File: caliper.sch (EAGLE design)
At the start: 57 parts, among them IC1 AT90S2313S, IC3 TS5205, IC6 MAX489CSD, Q10 BCX71SMD, Q11 BCX71SMD, Q12 BC817-40SMD, Q13 BC817-40SMD, Q2 BCX71SMD, Q3 BCX71SMD, Q4 BC817-40SMD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

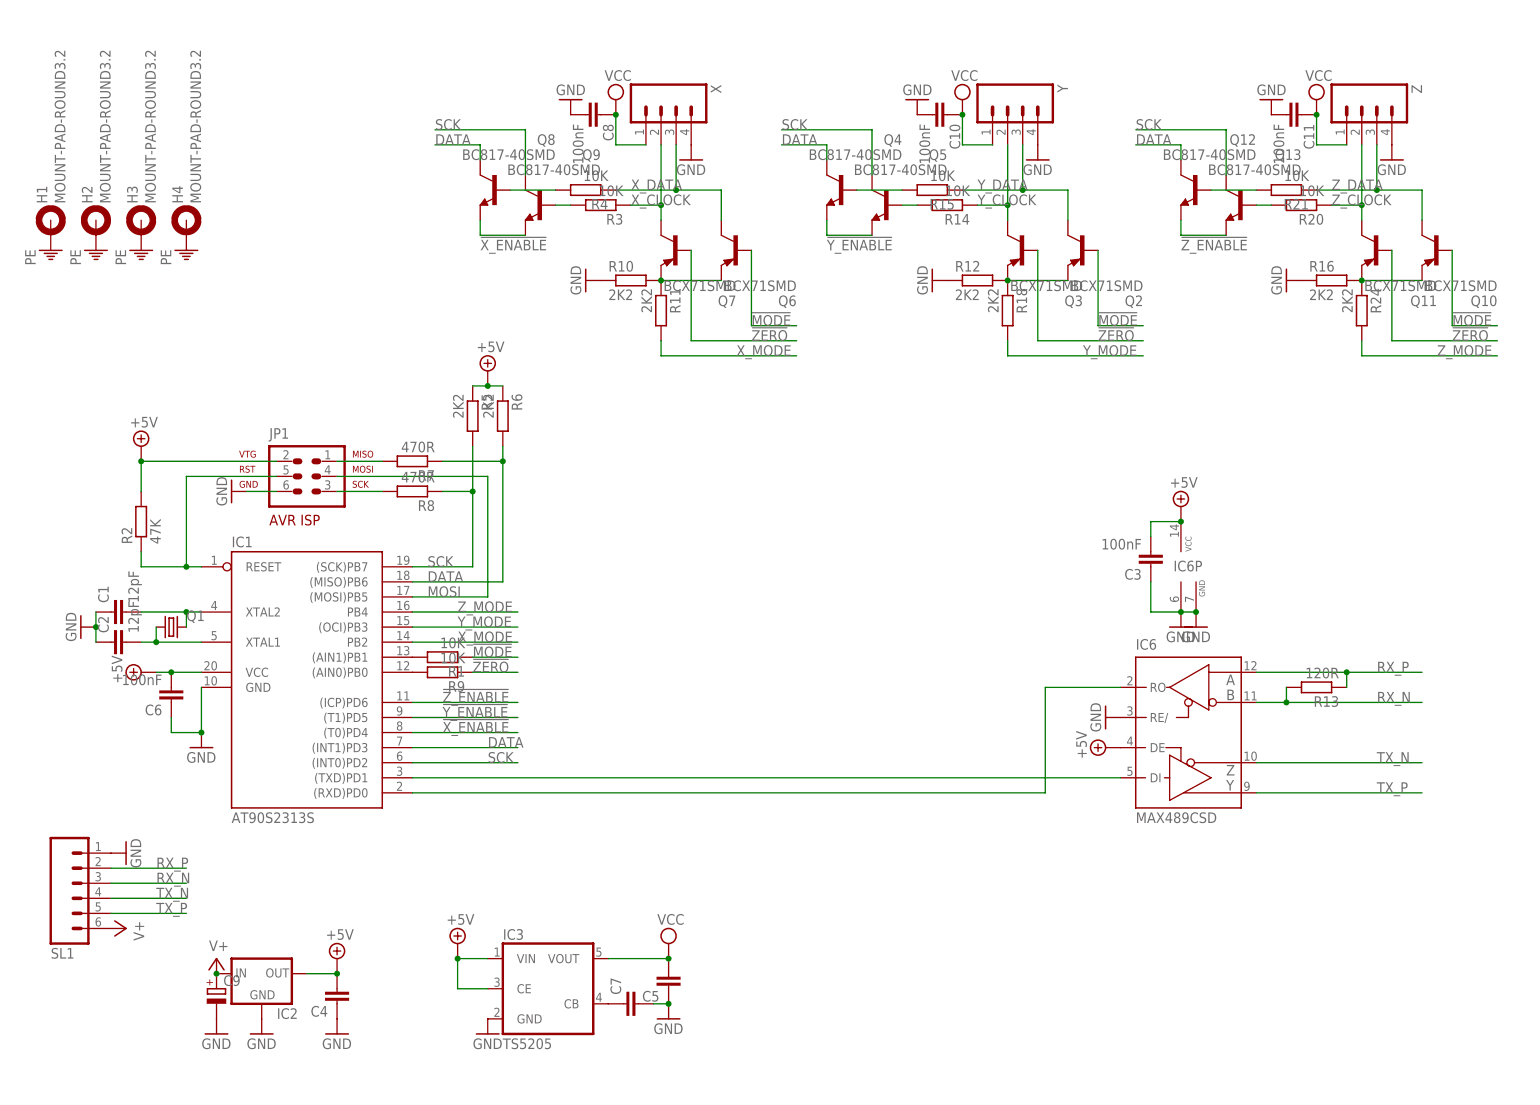
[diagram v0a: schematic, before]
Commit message: switch to ATmega88 & spi readout, Board & schematic ready
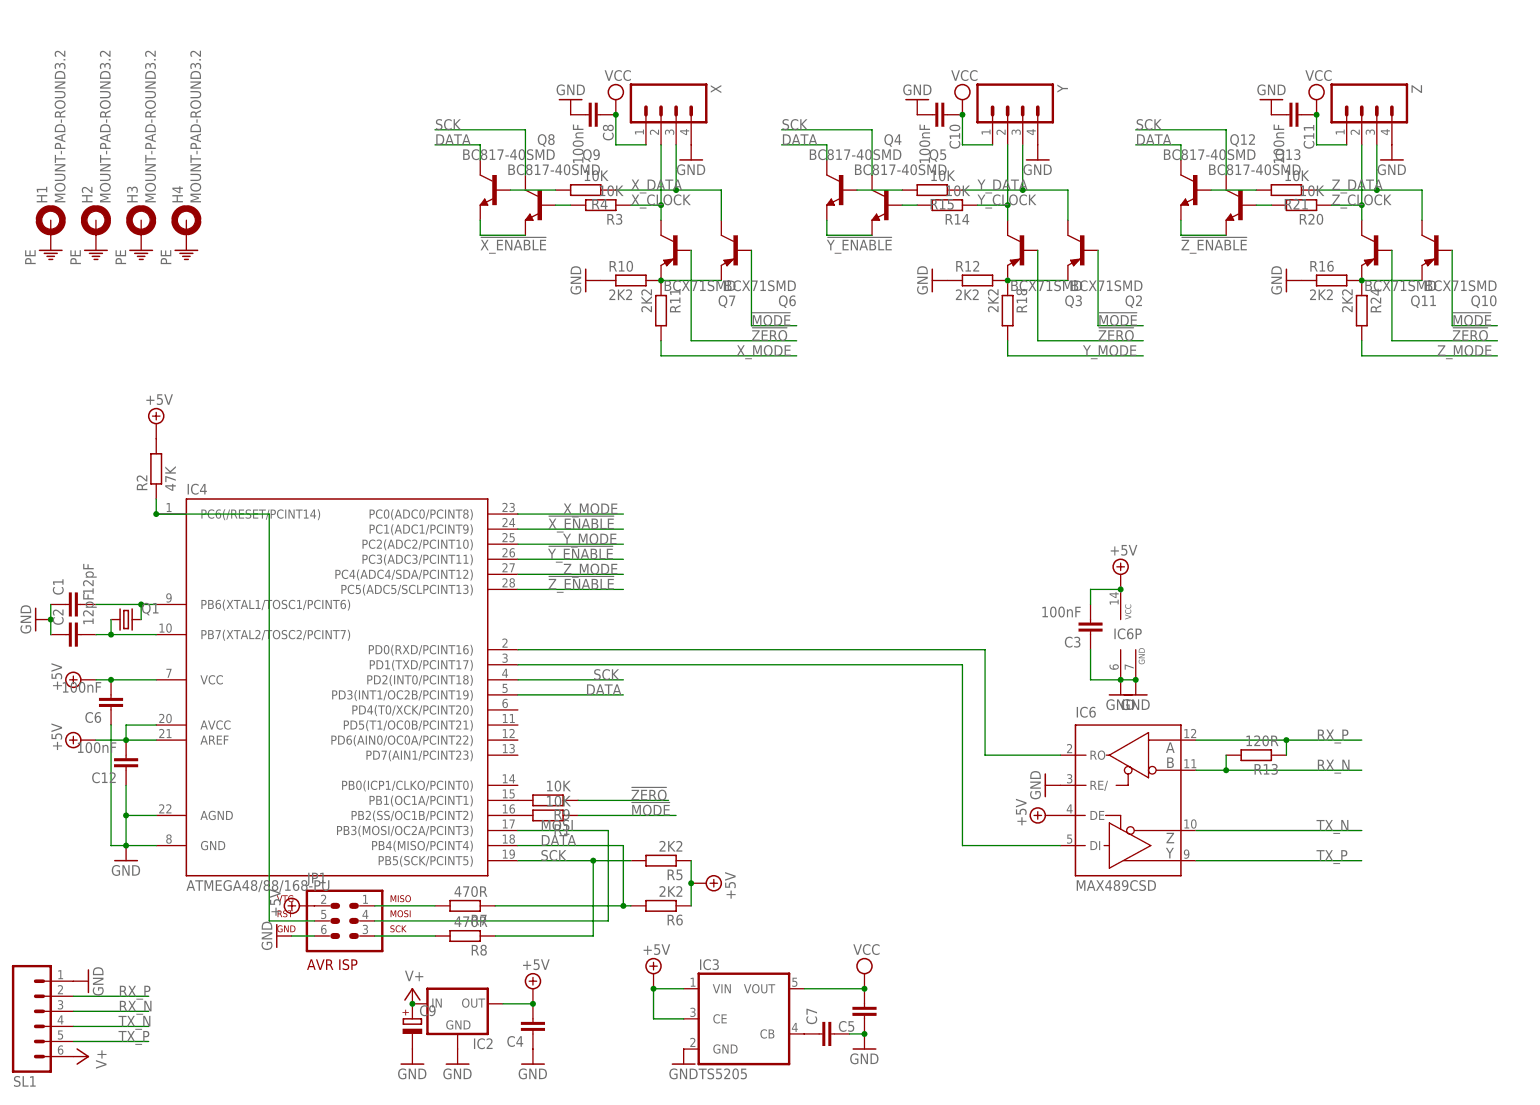
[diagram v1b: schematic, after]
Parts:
- removed IC1: AT90S2313S, atmel:AT90S2313S
- added C12: 100nF, rcl:C-EUC0805
- added IC4: ATMEGA48/88/168-PU, atmega8:ATMEGA48/88/168-PU
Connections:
- net !X_ENABLE: now also IC4.PC1(ADC1/PCINT9); no longer IC1.(T0)PD4
- net !Y_ENABLE: now also IC4.PC3(ADC3/PCINT11); no longer IC1.(T1)PD5
- net !Z_ENABLE: now also IC4.PC5(ADC5/SCLPCINT13); no longer IC1.(ICP)PD6
- net +5V: now also C12.2, IC4.AREF, IC4.AVCC, IC4.VCC@1; no longer IC1.VCC
- net DATA: now also IC4.PB4(MISO/PCINT4), IC4.PD3(INT1/OC2B/PCINT19); no longer IC1.(INT1)PD3, IC1.(MISO)PB6
- net GND: now also C12.1, IC4.AGND, IC4.GND@1; no longer IC1.GND
- net MOSI: now also IC4.PB3(MOSI/OC2A/PCINT3); no longer IC1.(MOSI)PB5
- net N$1: now also IC4.PB6(XTAL1/TOSC1/PCINT6); no longer IC1.XTAL2
- net N$2: now also IC4.PB7(XTAL2/TOSC2/PCINT7); no longer IC1.XTAL1
- net N$3: now also IC4.PD0(RXD/PCINT16); no longer IC1.(RXD)PD0
- net N$4: now also IC4.PD1(TXD/PCINT17); no longer IC1.(TXD)PD1
- net N$6: now also IC4.PB1(OC1A/PCINT1); no longer IC1.(AIN0)PB0
- net N$7: now also IC4.PC6(/RESET/PCINT14); no longer IC1.RESET
- net N$8: now also IC4.PB2(SS/OC1B/PCINT2); no longer IC1.(AIN1)PB1
- net SCK: now also IC4.PB5(SCK/PCINT5), IC4.PD2(INT0/PCINT18); no longer IC1.(INT0)PD2, IC1.(SCK)PB7
- net X_MODE: now also IC4.PC0(ADC0/PCINT8); no longer IC1.PB2
- net Y_MODE: now also IC4.PC2(ADC2/PCINT10); no longer IC1.(OCI)PB3
- net Z_MODE: now also IC4.PC4(ADC4/SDA/PCINT12); no longer IC1.PB4
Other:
- moved on the sheet: C1, C2, C3, C4, C5, C6, C7, C9, IC2, IC3, IC6, IC6P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
